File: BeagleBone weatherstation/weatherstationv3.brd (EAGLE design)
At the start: 86.4 x 38.1 mm, 10 parts, among them P2 CONN23-2FB

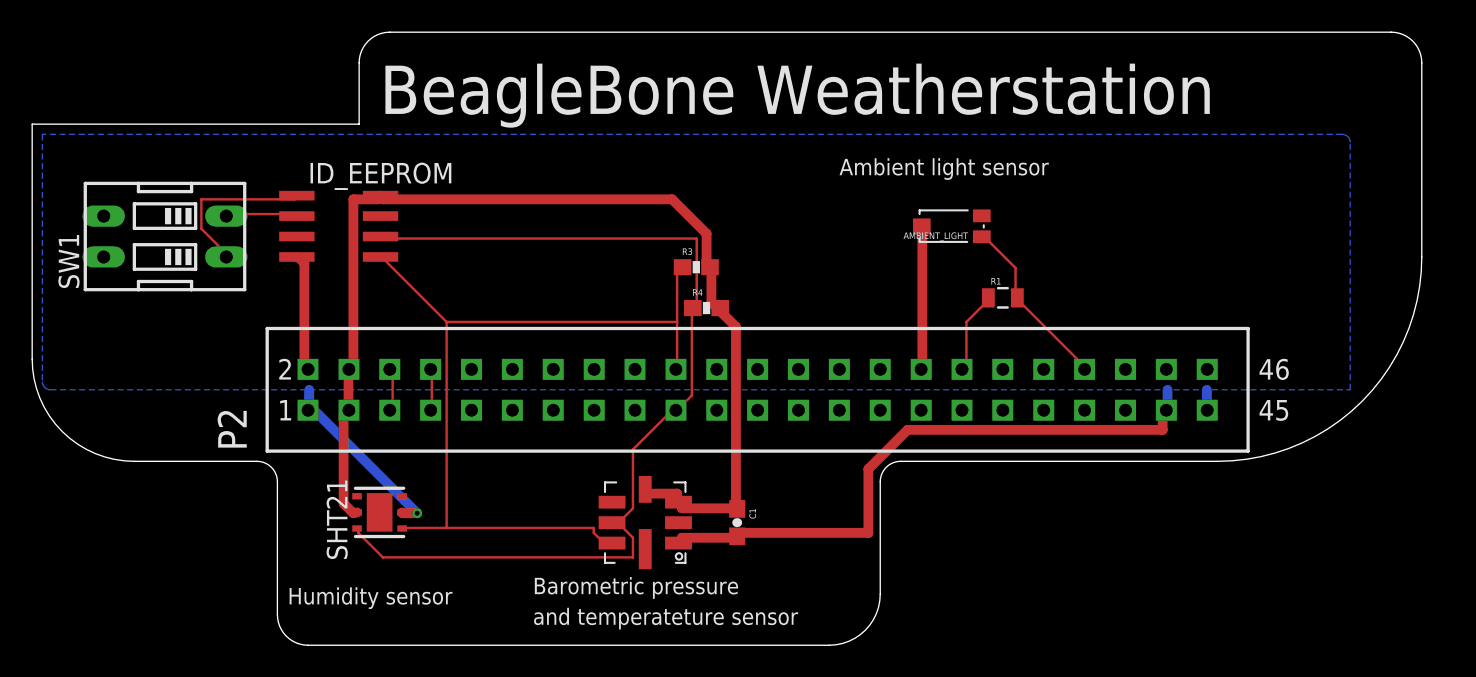
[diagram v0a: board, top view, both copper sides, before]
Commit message: weatherstation: add missing EEPROM address pullups into v3 schematic and board
Signed-off-by: Koen Kooi <koen@dominion.thruhere.net>
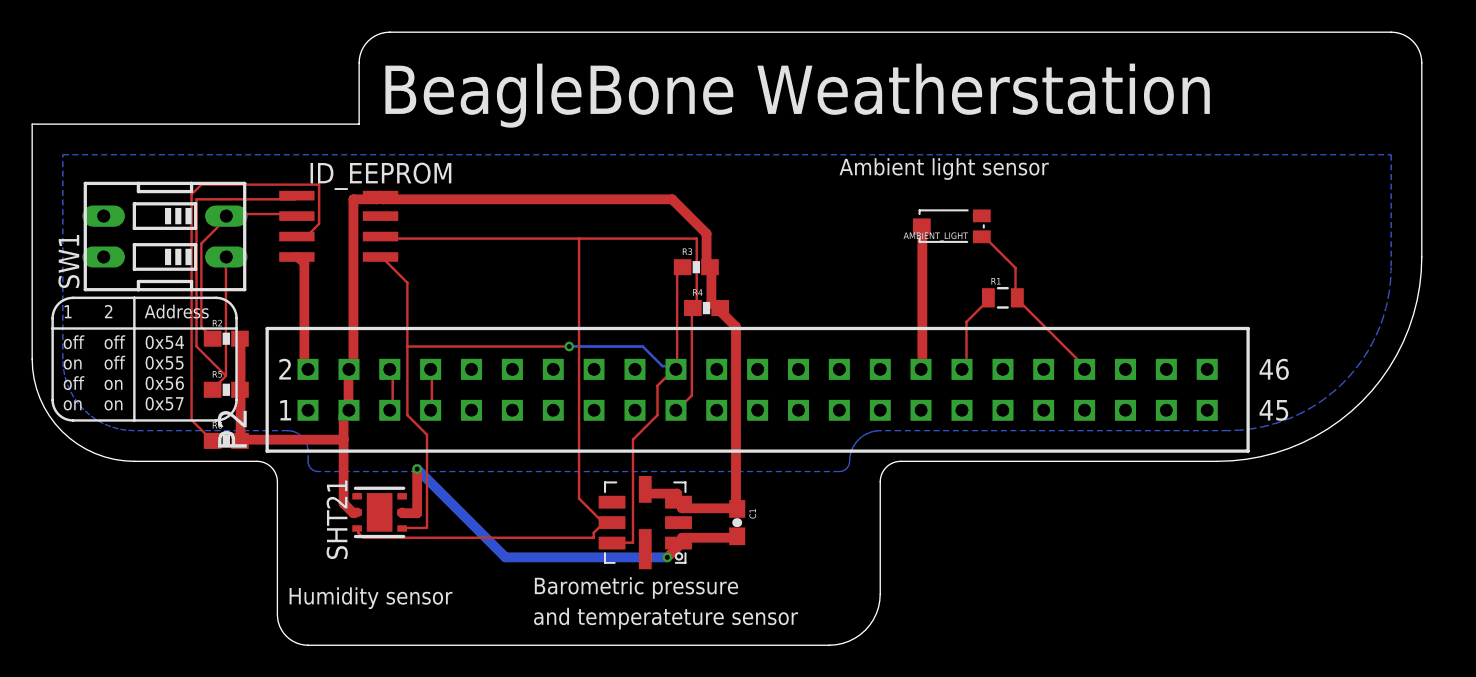
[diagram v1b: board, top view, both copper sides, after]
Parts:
- added R2, R5, R6: 4.7k, SparkFun:0603-RES
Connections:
- net N$1: now also R5.1
- net N$6: now also R6.1
- net N$7: now also R2.1
- net VDD_3V3EXP: now also R2.2, R5.2, R6.2
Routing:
- net N$6: track 0.00 -> 28.2 mm
- net DGND: track 58.6 -> 34.0 mm, vias 1 -> 2
- net N$1: track 10.3 -> 26.7 mm
- net VDD_3V3EXP: track 68.0 -> 80.8 mm
- net N$7: track 4.46 -> 13.0 mm
- net I2C2_SCL: track 61.4 -> 67.0 mm
- net I2C2_SDA: track 53.3 -> 56.6 mm, vias 0 -> 1
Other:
- board text added: "0x54"
- board text added: "0x55"
- board text added: "0x56"
- board text added: "0x57"
- board text added: "Address"
- board text added: "off"
- board text added: "on"

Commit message: weatherstation: fix typo reported by Steve Sakoman, move EEPROM pullups around
Signed-off-by: Koen Kooi <koen@dominion.thruhere.net>
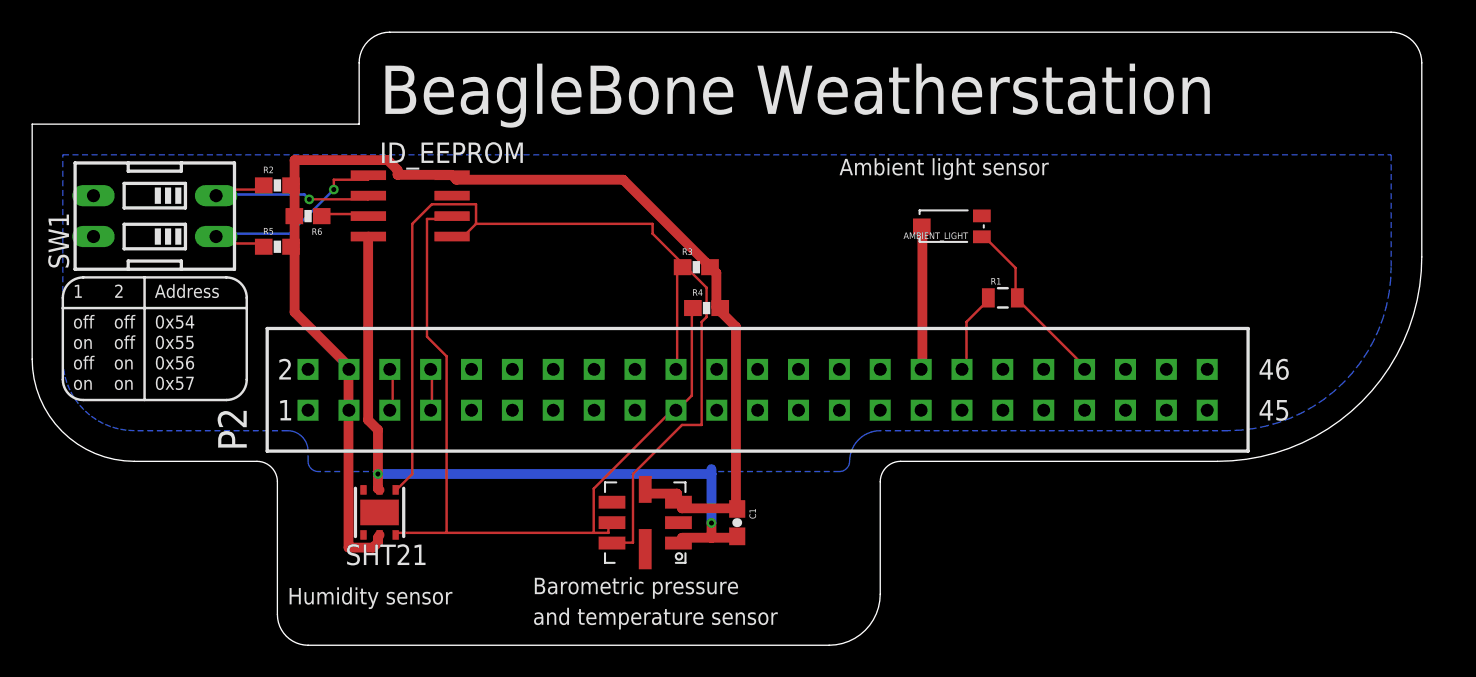
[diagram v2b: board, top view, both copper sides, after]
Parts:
- moved R6 14.9 mm to (21.0, 34.9), turned to 180 degrees
- moved R2 10.0 mm to (19.1, 36.8)
- moved R5 9.44 mm to (19.1, 33.0)
- moved ID_EEPROM 4.62 mm to (27.3, 35.6)
- moved SW1 1.42 mm to (11.4, 34.9)
- turned SHT21 to 180 degrees
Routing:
- net N$6: track 28.2 -> 3.06 mm
- net I2C2_SCL: track 67.0 -> 52.5 mm
- net N$1: track 26.7 -> 15.1 mm, vias 0 -> 1
- net DGND: track 34.0 -> 45.0 mm
- net I2C2_SDA: track 56.6 -> 67.1 mm, vias 1 -> 0
- net VDD_3V3EXP: track 80.8 -> 79.7 mm
- net N$7: track 13.0 -> 13.3 mm, vias 0 -> 1
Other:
- board text added: "and temperature sensor"
- board text removed: "and temperateture sensor"

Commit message: weatherstation: cut away some more PCB around the sensors
Signed-off-by: Koen Kooi <koen@dominion.thruhere.net>
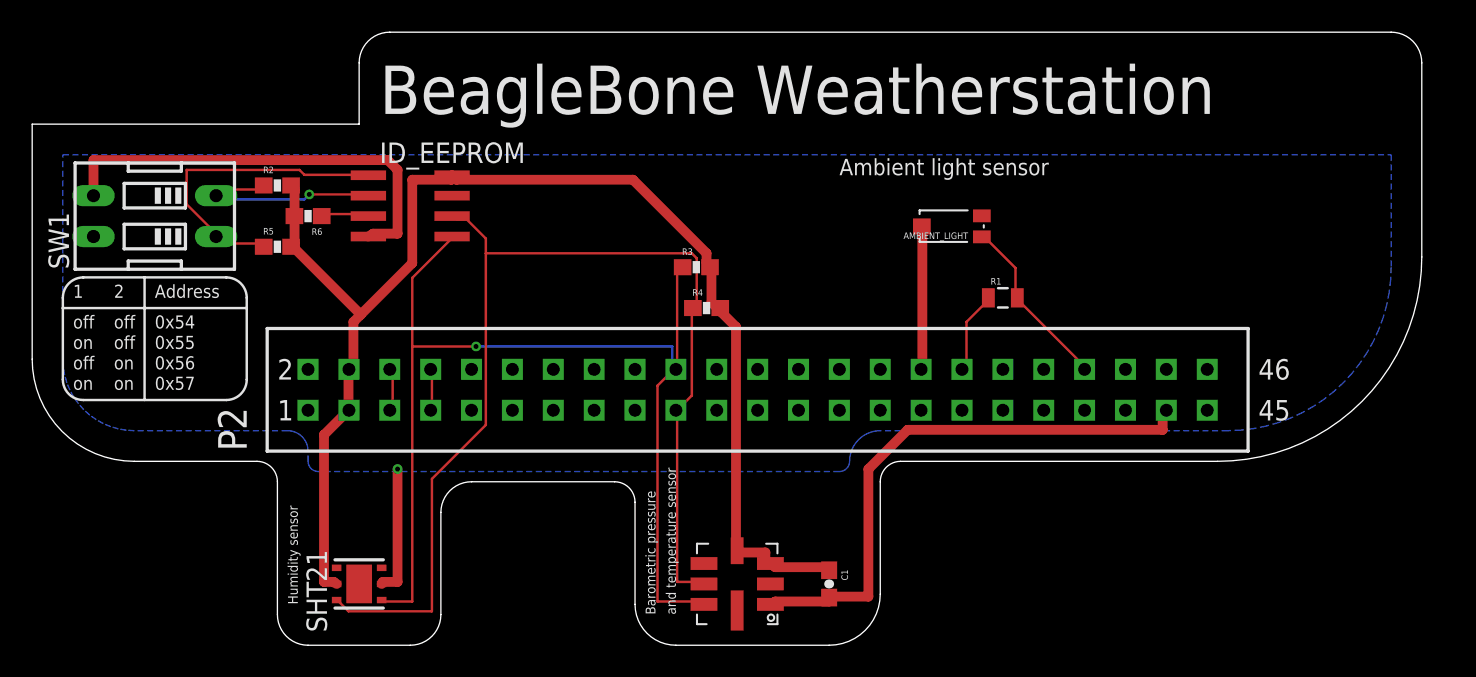
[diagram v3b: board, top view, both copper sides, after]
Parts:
- SHT21: value SHT2x -> (none)
- moved BAROMETRIC_PRESSURE 6.87 mm to (47.6, 12.1)
- moved C1 6.87 mm to (53.3, 12.1)
- moved SHT21 4.62 mm to (24.1, 12.1), turned to 90 degrees
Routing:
- net DGND: track 45.0 -> 70.4 mm, vias 2 -> 1
- net I2C2_SCL: track 52.5 -> 69.1 mm
- net VDD_3V3EXP: track 79.7 -> 84.7 mm
- net N$1: track 15.1 -> 19.8 mm, vias 1 -> 0
- net I2C2_SDA: track 67.1 -> 67.8 mm, vias 0 -> 1
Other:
- outline, holes or cut-outs redrawn
